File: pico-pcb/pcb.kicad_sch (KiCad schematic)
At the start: 25 parts, among them J1 AudioJack1, J2 AudioJack2, Q1 2N3904, SW1 SW_DIP_x04, U1 Pico

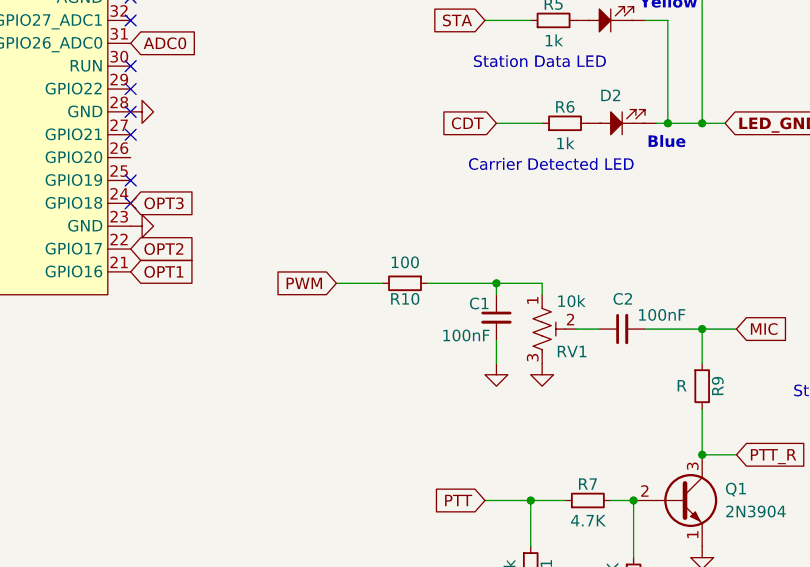
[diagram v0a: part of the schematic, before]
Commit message: Modified schematic and bom for more readable R10 100Ohm and R9 optional resistor
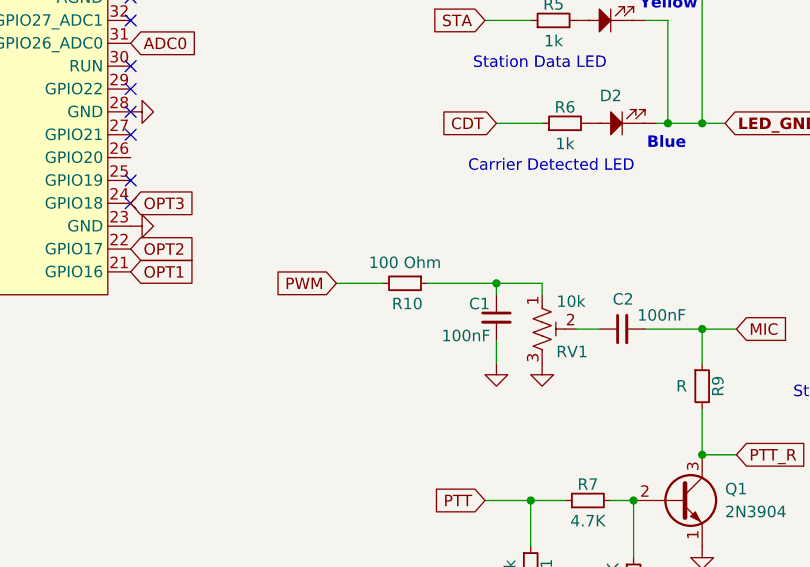
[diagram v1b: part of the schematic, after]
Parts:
- R10: value 100 -> 100 Ohm
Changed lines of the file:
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@@
 		(dnp no)
 		(property "Reference" "R10"
-			(at 133.35 130.048 90)
+			(at 133.604 130.556 90)
 			(effects
 				(font
@@
 			)
 		)
-		(property "Value" "100"
+		(property "Value" "100 Ohm"
 			(at 133.35 125.984 90)
 			(effects
 				(font
 					(size 1.27 1.27)
+					(thickness 0.1588)
 				)
 			)
